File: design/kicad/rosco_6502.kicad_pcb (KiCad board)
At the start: 4 copper layers, 100 x 100 mm, 55 parts, among them IC1 W65C02SxP, IC2 ATF22V10C-7PX, IC3 XR68C681CJTR-F, IC4 NE555P, IC5 ATF22V10C-7PX, J1 UART_A, J2 UART_B, J3 Conn_01x06, J4 Conn_01x01_Male, J5 Conn_02x18_Odd_Even, J6 Conn_01x02_Male, Q1 3.6864MHz, U1 AS6C4008-55PCN, U2 AS6C62256-55PCN, U3 AT28C64B-15PU, U4 74HCT174, X1 14MHz

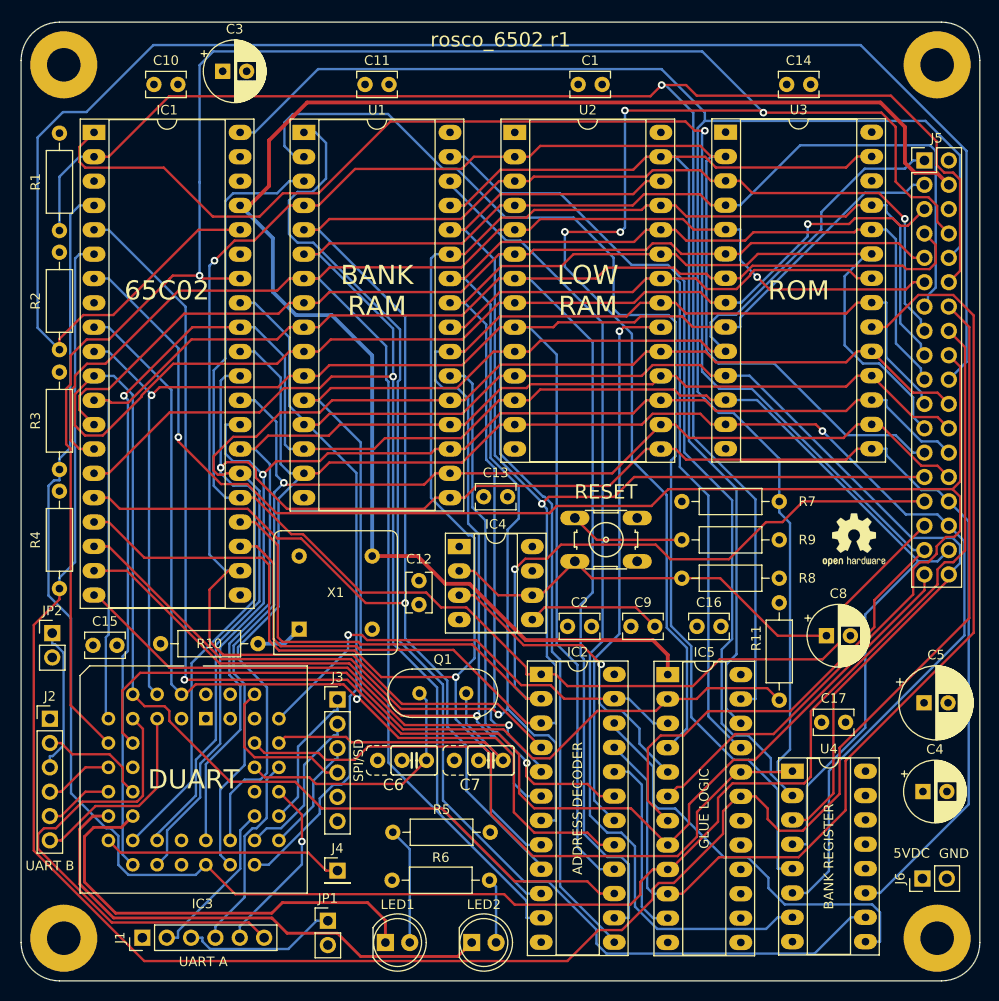
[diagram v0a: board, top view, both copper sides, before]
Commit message: Stretch timing for BANKSEL via glue
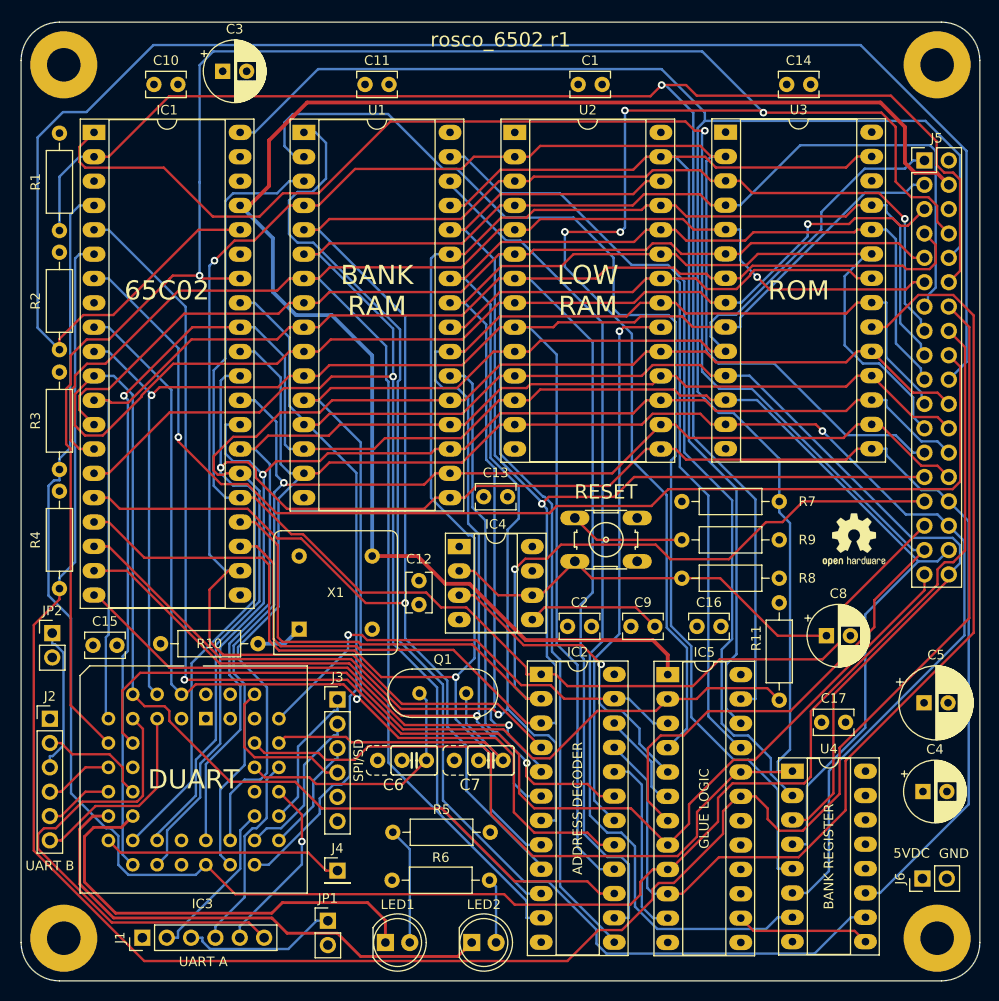
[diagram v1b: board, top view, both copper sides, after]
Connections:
- IC5 pad 14: unconnected-(IC5-Pad14) -> BANKCLK
- IC5 pad 6: SYNC -> BANKSEL
- U4 pad 9: BANKSEL -> BANKCLK
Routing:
- net SYNC: track 169.9 -> 121.2 mm
- net BANKSEL: track 43.2 -> 9.51 mm
- net BANKCLK: track 0.00 -> 14.0 mm
- net BANK1: track 122.4 -> 121.5 mm
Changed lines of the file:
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@@
   (net 74 "Net-(C9-Pad2)")
   (net 75 "unconnected-(IC5-Pad13)")
-  (net 76 "unconnected-(IC5-Pad14)")
+  (net 76 "BANKCLK")
   (net 77 "unconnected-(IC5-Pad15)")
   (net 78 "unconnected-(IC5-Pad16)")
@@
       (net 1 "GND") (pinfunction "GND") (pintype "power_in"))
     (pad "9" thru_hole oval locked (at 7.62 17.78) (size 2.4 1.6) (drill 0.8) (layers *.Cu *.Mask)
-      (net 47 "BANKSEL") (pinfunction "Cp") (pintype "input"))
+      (net 76 "BANKCLK") (pinfunction "Cp") (pintype "input"))
     (pad "10" thru_hole oval locked (at 7.62 15.24) (size 2.4 1.6) (drill 0.8) (layers *.Cu *.Mask)
       (net 90 "BANK3") (pinfunction "Q3") (pintype "output"))
@@
       (net 72 "HWRST") (pinfunction "I5") (pintype "input"))
     (pad "6" thru_hole oval locked (at 0 12.7) (size 2.4 1.6) (drill 0.8) (layers *.Cu *.Mask)
-      (net 17 "SYNC") (pinfunction "I6") (pintype "input"))
+      (net 47 "BANKSEL") (pinfunction "I6") (pintype "input"))
     (pad "7" thru_hole oval locked (at 0 15.24) (size 2.4 1.6) (drill 0.8) (layers *.Cu *.Mask)
       (net 6 "~{VP}") (pinfunction "I7") (pintype "input"))
@@
       (net 75 "unconnected-(IC5-Pad13)") (pinfunction "I13") (pintype "input+no_connect"))
     (pad "14" thru_hole oval locked (at 7.62 25.4) (size 2.4 1.6) (drill 0.8) (layers *.Cu *.Mask)
-      (net 76 "unconnected-(IC5-Pad14)") (pinfunction "IO1") (pintype "bidirectional+no_connect"))
+      (net 76 "BANKCLK") (pinfunction "IO1") (pintype "bidirectional"))
     (pad "15" thru_hole oval locked (at 7.62 22.86) (size 2.4 1.6) (drill 0.8) (layers *.Cu *.Mask)
       (net 77 "unconnected-(IC5-Pad15)") (pinfunction "IO2") (pintype "bidirectional+no_connect"))
@@
   (segment (start 169.37 124.6952) (end 169.37 129.5029) (width 0.25) (layer "F.Cu") (net 15))
   (segment (start 85.3216 135.41) (end 96.8424 146.9308) (width 0.25) (layer "F.Cu") (net 15))
-  (segment (start 158.765 129.755) (end 159.07 129.755) (width 0.25) (layer "F.Cu") (net 15))
   (segment (start 157.22 131.3) (end 158.765 129.755) (width 0.25) (layer "F.Cu") (net 15))
   (segment (start 88 109.2053) (end 85.3216 111.8837) (width 0.25) (layer "F.Cu") (net 15))
@@
   (segment (start 108.8598 97.898482) (end 107.021318 96.06) (width 0.25) (layer "B.Cu") (net 16))
   (segment (start 104.8574 97.1854) (end 107.5959 97.1854) (width 0.25) (layer "F.Cu") (net 17))
-  (segment (start 152.9753 128.775) (end 158.4899 123.2604) (width 0.25) (layer "F.Cu") (net 17))
   (segment (start 100.4065 92.7345) (end 104.8574 97.1854) (width 0.25) (layer "F.Cu") (net 17))
-  (segment (start 179.495 104.4598) (end 179.495 103.6707) (width 0.25) (layer "F.Cu") (net 17))
   (segment (start 107.5959 97.1854) (end 110.6256 100.2151) (width 0.25) (layer "F.Cu") (net 17))
   (segment (start 181.9663 84.9463) (end 180.765 83.745) (width 0.25) (layer "F.Cu") (net 17))
-  (segment (start 181.325 102.7003) (end 181.9553 102.07) (width 0.25) (layer "F.Cu") (net 17))
-  (segment (start 152.9753 128.775) (end 152.43 128.775) (width 0.25) (layer "F.Cu") (net 17))
   (segment (start 151.5041 97.7124) (end 181.1601 97.7124) (width 0.25) (layer "F.Cu") (net 17))
   (segment (start 110.6256 100.2151) (end 139.1046 100.2151) (width 0.25) (layer "F.Cu") (net 17))
-  (segment (start 179.495 103.6707) (end 180.4654 102.7003) (width 0.25) (layer "F.Cu") (net 17))
-  (segment (start 152.43 128.775) (end 151.45 129.755) (width 0.25) (layer "F.Cu") (net 17))
-  (segment (start 177.0497 106.0219) (end 177.7366 105.335) (width 0.25) (layer "F.Cu") (net 17))
-  (segment (start 181.9553 102.07) (end 181.9553 98.5076) (width 0.25) (layer "F.Cu") (net 17))
-  (segment (start 180.4654 102.7003) (end 181.325 102.7003) (width 0.25) (layer "F.Cu") (net 17))
-  (segment (start 177.0497 108.6863) (end 177.0497 106.0219) (width 0.25) (layer "F.Cu") (net 17))
-  (segment (start 158.4899 123.2604) (end 162.4756 123.2604) (width 0.25) (layer "F.Cu") (net 17))
   (segment (start 100.4065 92.2904) (end 100.4065 92.7345) (width 0.25) (layer "F.Cu") (net 17))
   (segment (start 139.8521 99.4676) (end 149.7489 99.4676) (width 0.25) (layer "F.Cu") (net 17))
@@
   (segment (start 139.1046 100.2151) (end 139.8521 99.4676) (width 0.25) (layer "F.Cu") (net 17))
   (segment (start 181.1601 97.7124) (end 181.9663 96.9062) (width 0.25) (layer "F.Cu") (net 17))
-  (segment (start 162.4756 123.2604) (end 177.0497 108.6863) (width 0.25) (layer "F.Cu") (net 17))
-  (segment (start 181.9553 98.5076) (end 181.1601 97.7124) (width 0.25) (layer "F.Cu") (net 17))
-  (segment (start 177.7366 105.335) (end 178.6198 105.335) (width 0.25) (layer "F.Cu") (net 17))
   (segment (start 181.9663 96.9062) (end 181.9663 84.9463) (width 0.25) (layer "F.Cu") (net 17))
-  (segment (start 178.6198 105.335) (end 179.495 104.4598) (width 0.25) (layer "F.Cu") (net 17))
   (via (at 100.4065 92.2904) (size 0.8) (drill 0.4) (layers "F.Cu" "B.Cu") (net 17))
   (segment (start 100.4065 83.0129) (end 100.4065 92.2904) (width 0.25) (layer "B.Cu") (net 17))
@@
   (segment (start 115.7643 125.9397) (end 118.8074 125.9397) (width 0.25) (layer "F.Cu") (net 42))
   (segment (start 154.5024 131.3777) (end 158.6651 127.215) (width 0.25) (layer "F.Cu") (net 42))
-  (segment (start 164.365 127.215) (end 164.45 127.13) (width 0.25) (layer "F.Cu") (net 42))
   (segment (start 159.07 127.215) (end 164.365 127.215) (width 0.25) (layer "F.Cu") (net 42))
   (segment (start 109.3865 125.2265) (end 115.0511 125.2265) (width 0.25) (layer "F.Cu") (net 42))
@@
   (segment (start 149.3062 128.0862) (end 145.87 124.65) (width 0.25) (layer "B.Cu") (net 46))
   (segment (start 149.3062 139.2965) (end 149.3062 128.0862) (width 0.25) (layer "B.Cu") (net 46))
-  (segment (start 149.9247 130.510971) (end 150.438729 131.025) (width 0.25) (layer "B.Cu") (net 47))
-  (segment (start 173.5953 144.91) (end 172.07 144.91) (width 0.25) (layer "B.Cu") (net 47))
-  (segment (start 152.2312 131.025) (end 157.3112 136.105) (width 0.25) (layer "B.Cu") (net 47))
-  (segment (start 173.5953 141.8517) (end 173.5953 144.91) (width 0.25) (layer "B.Cu") (net 47))
-  (segment (start 159.8023 136.105) (end 161.9471 138.2498) (width 0.25) (layer "B.Cu") (net 47))
-  (segment (start 145.87 122.5847) (end 149.9247 126.6394) (width 0.25) (layer "B.Cu") (net 47))
-  (segment (start 149.9247 126.6394) (end 149.9247 130.510971) (width 0.25) (layer "B.Cu") (net 47))
-  (segment (start 157.3112 136.105) (end 159.8023 136.105) (width 0.25) (layer "B.Cu") (net 47))
-  (segment (start 161.9471 139.3187) (end 163.6545 141.0261) (width 0.25) (layer "B.Cu") (net 47))
-  (segment (start 161.9471 138.2498) (end 161.9471 139.3187) (width 0.25) (layer "B.Cu") (net 47))
-  (segment (start 163.6545 141.0261) (end 172.7697 141.0261) (width 0.25) (layer "B.Cu") (net 47))
-  (segment (start 150.438729 131.025) (end 152.2312 131.025) (width 0.25) (layer "B.Cu") (net 47))
-  (segment (start 172.7697 141.0261) (end 173.5953 141.8517) (width 0.25) (layer "B.Cu") (net 47))
+  (segment (start 149.75572 128.74) (end 150.77072 129.755) (width 0.25) (layer "B.Cu") (net 47))
+  (segment (start 145.87 122.270717) (end 149.75572 126.156438) (width 0.25) (layer "B.Cu") (net 47))
+  (segment (start 149.75572 126.156438) (end 149.75572 128.74) (width 0.25) (layer "B.Cu") (net 47))
   (segment (start 139.2262 118.1554) (end 136.1765 118.1554) (width 0.25) (layer "F.Cu") (net 48))
   (segment (start 136.1765 118.1554) (end 131.4737 113.4526) (width 0.25) (layer "F.Cu") (net 48))
@@
   (segment (start 148.12 110.04) (end 150.11 112.03) (width 0.25) (layer "F.Cu") (net 74))
   (segment (start 138.6 110.04) (end 148.12 110.04) (width 0.25) (layer "F.Cu") (net 74))
+  (segment (start 170.94548 143.78548) (end 172.07 144.91) (width 0.25) (layer "F.Cu") (net 76))
+  (segment (start 159.07 142.455) (end 160.40048 143.78548) (width 0.25) (layer "F.Cu") (net 76))
+  (segment (start 160.40048 143.78548) (end 170.94548 143.78548) (width 0.25) (layer "F.Cu") (net 76))
   (segment (start 155.3461 63.04) (end 150.7317 63.04) (width 0.25) (layer "F.Cu") (net 81))
   (segment (start 170.0549 64.1581) (end 156.4642 64.1581) (width 0.25) (layer "F.Cu") (net 81))
@@
   (segment (start 111.47 61.93) (end 111.47 59.46) (width 0.25) (layer "B.Cu") (net 91))
   (segment (start 152.257 80.2761) (end 152.257 94.2603) (width 0.25) (layer "B.Cu") (net 91))
-  (segment (start 113.5 63.04) (end 112.58 63.04) (width 0.25) (layer "B.Cu") (net 91))
   (segment (start 162.9247 137.29) (end 164.45 137.29) (width 0.25) (layer "B.Cu") (net 91))
   (segment (start 145.8 78.9018) (end 146.4482 79.55) (width 0.25) (layer "B.Cu") (net 91))

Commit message: Speedier ROM fixes
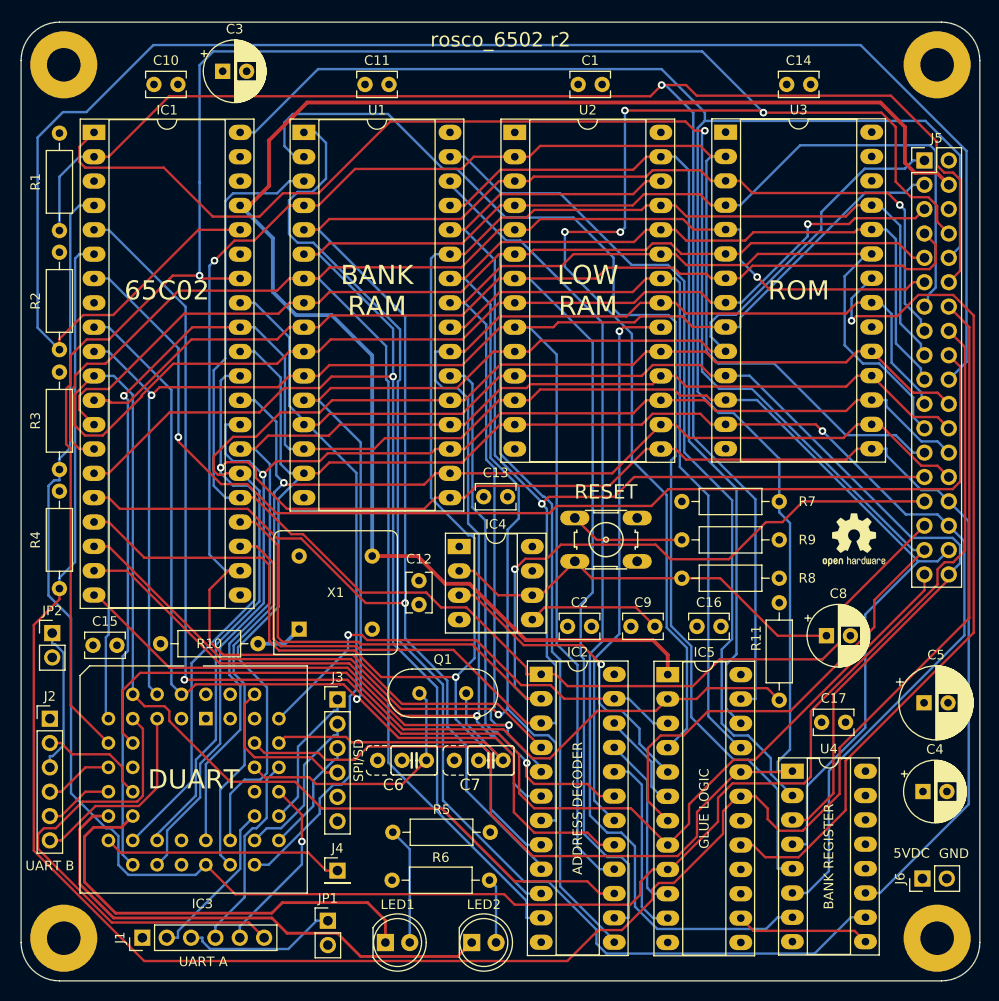
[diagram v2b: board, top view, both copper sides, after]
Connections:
- IC5 pad 17: unconnected-(IC5-Pad17) -> ~{ROMOE}
- U3 pad 20: ~{ROM} -> GND
- U3 pad 22: ~{RD} -> ~{ROMOE}
- U3 pad 27: ~{WR} -> VCC
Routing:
- net ~{ROM}: track 110.7 -> 18.5 mm
- net ~{ROMOE}: track 0.00 -> 90.7 mm, vias 0 -> 1
- net ~{RD}: track 100.3 -> 76.6 mm
- net ~{WR}: track 110.2 -> 87.7 mm
- net A10: track 161.1 -> 159.9 mm
- net A2: track 202.3 -> 201.6 mm
- net A7: track 193.1 -> 193.6 mm
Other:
- board text added: "rosco_6502 r2"
- board text removed: "rosco_6502 r1"

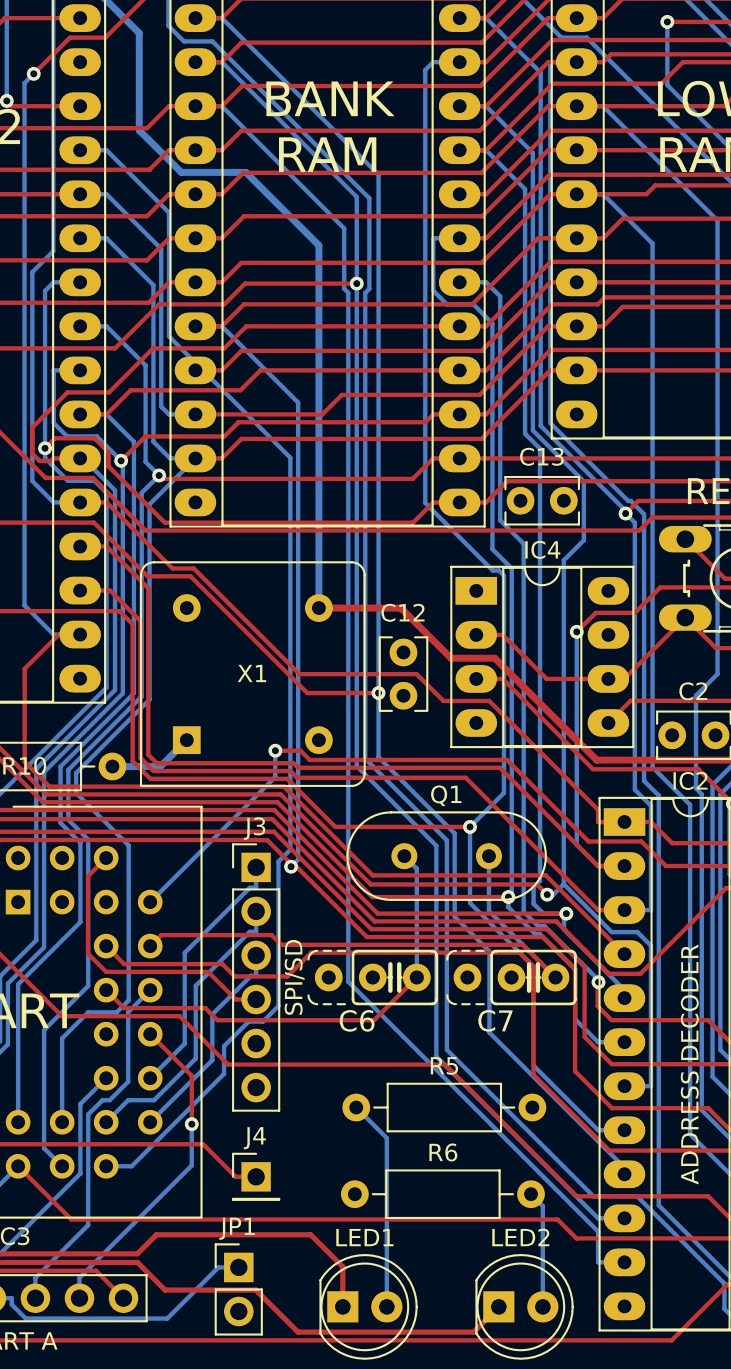
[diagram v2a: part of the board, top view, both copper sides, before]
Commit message: Add missing DUART IACK pullup
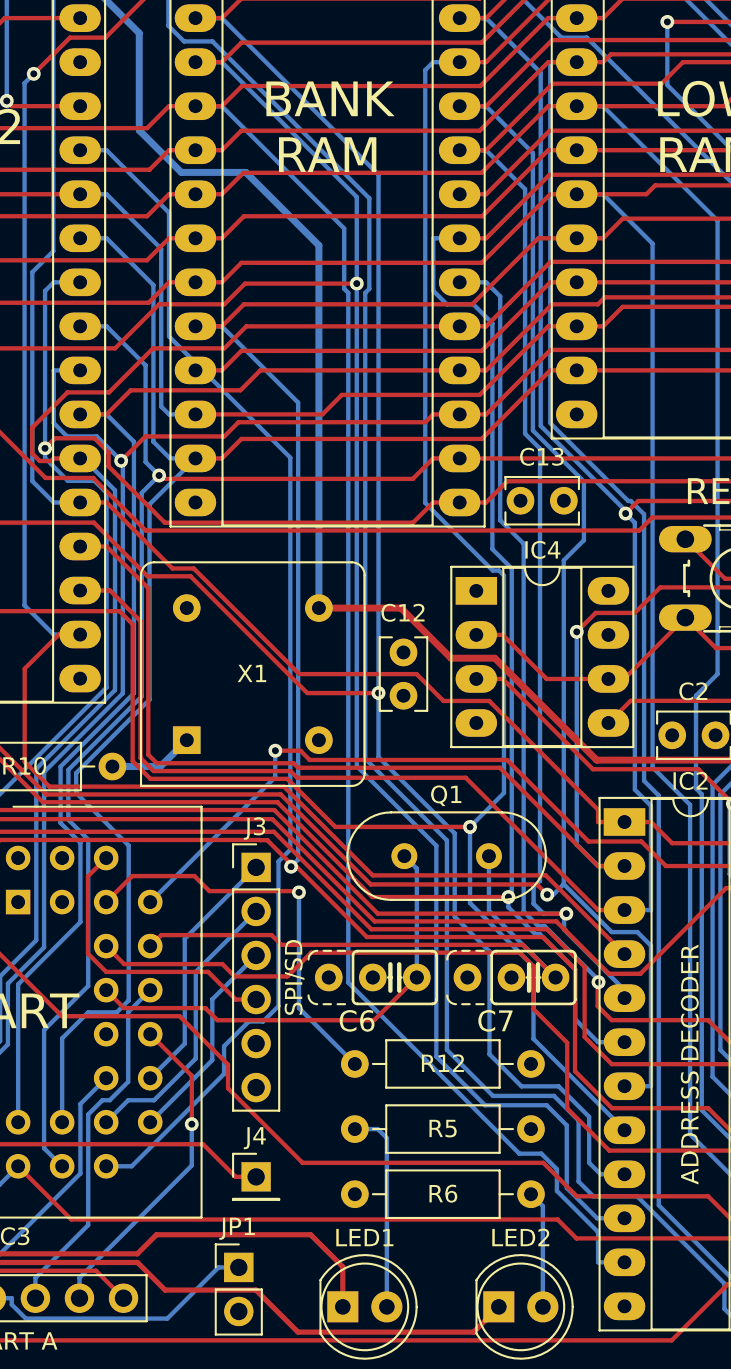
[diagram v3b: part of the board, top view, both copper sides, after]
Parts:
- added R12: 3K3, Resistor_THT:R_Axial_DIN0207_L6.3mm_D2.5mm_P10.16mm_Horizontal, F.Cu at (132.9, 131.0)
- R10: value 4K7 -> 3K3
- moved R5 1.25 mm to (122.7, 134.7)
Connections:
- IC3 pad 41: unconnected-(IC3-Pad41) -> Net-(IC3-Pad41)
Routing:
- net Net-(IC3-Pad41): track 0.00 -> 23.4 mm, vias 0 -> 1
- net A7: track 193.6 -> 196.1 mm
- net A6: track 202.1 -> 204.2 mm
- net BANK3: track 134.8 -> 136.8 mm
- net A8: track 184.8 -> 183.9 mm
- net A2: track 201.6 -> 202.4 mm
- net A5: track 188.6 -> 189.4 mm

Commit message: r3
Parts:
- added J7: Jack-DC, Connector_BarrelJack:BarrelJack_Horizontal, F.Cu at (169.3, 115.0)
- added REF**: Symbol_Barrel_Polarity, Symbol:Symbol_Barrel_Polarity, B.Cu at (181.6, 115.0)
- added REF**: RoHS-Logo_6mm_SilkScreen, Symbol:RoHS-Logo_6mm_SilkScreen, B.Cu at (121.1, 72.1)
- added rosco6502: rosco_6502, rosco_6502:rosco_6502, F.Cu at (132.4, 52.4)
- moved ohw 50.0 mm to (171.7, 53.0)
- moved C20 10.2 mm to (170.0, 103.0)
- moved C17 4.86 mm to (176.3, 124.5)
- moved C18 2.75 mm to (178.0, 132.0)
- moved C10 0.50 mm to (167.0, 122.0)
- renumbered C10 to C1, C17 to C10, C12 to C11, C2 to C12, C6 to C13, C7 to C14, C13 to C15, C3 to C16, C5 to C17, C4 to C18, C9 to C19, C11 to C2, C8 to C20, C1 to C3, C14 to C4, C16 to C8, C15 to C9, REF** to ohw
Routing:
- net IRQ: track 212.0 -> 216.8 mm
- net ~{ML}: track 152.4 -> 156.2 mm
- net ~{VP}: track 179.4 -> 182.1 mm
- net D1: track 195.7 -> 198.2 mm
- net A15: track 131.3 -> 129.4 mm
- net D0: track 185.3 -> 186.9 mm
- net Net-(C20-Pad1): track 43.1 -> 44.3 mm
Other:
- board text added: "5VDC Only!"
- board text added: "CIPO"
- board text added: "CK"
- board text added: "COPI"
- board text added: "CS"
- board text added: "CTS"
- board text added: "J1 - UART A"
- board text added: "RTS"
- board text added: "RxD"
- board text added: "TxD"
- board text added: "VCC"
- board text added: "r3"
- board text removed: "SPI/SD"
- board text removed: "UART A"
- board text removed: "rosco_6502 r2"
